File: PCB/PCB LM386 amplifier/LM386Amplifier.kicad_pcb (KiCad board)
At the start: 2 copper layers, 37.5 x 25.4 mm, 21 parts, among them J1 JACK_2P, P1 CONN_01X02, P2 CONN_01X02, U1 LM386

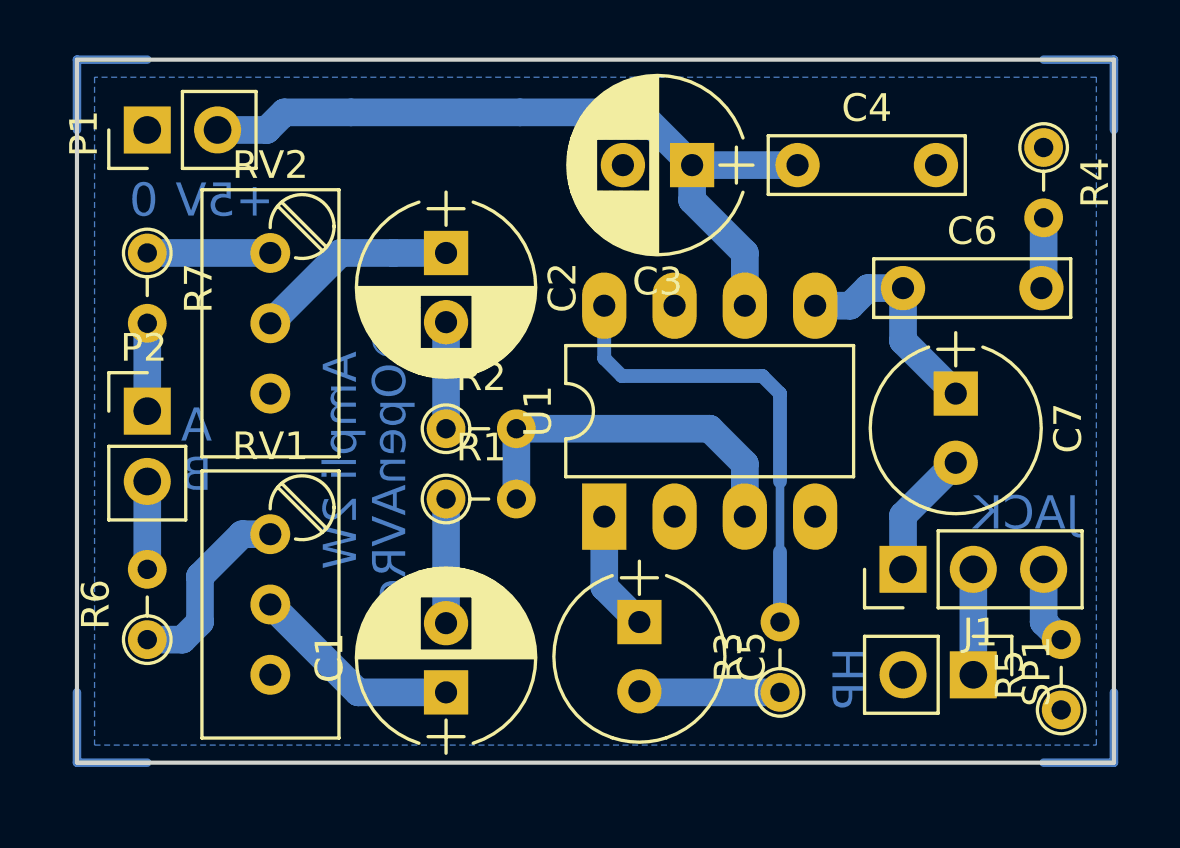
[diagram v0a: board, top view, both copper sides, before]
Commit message: Update pcb board
Add capacitor on pin 7.
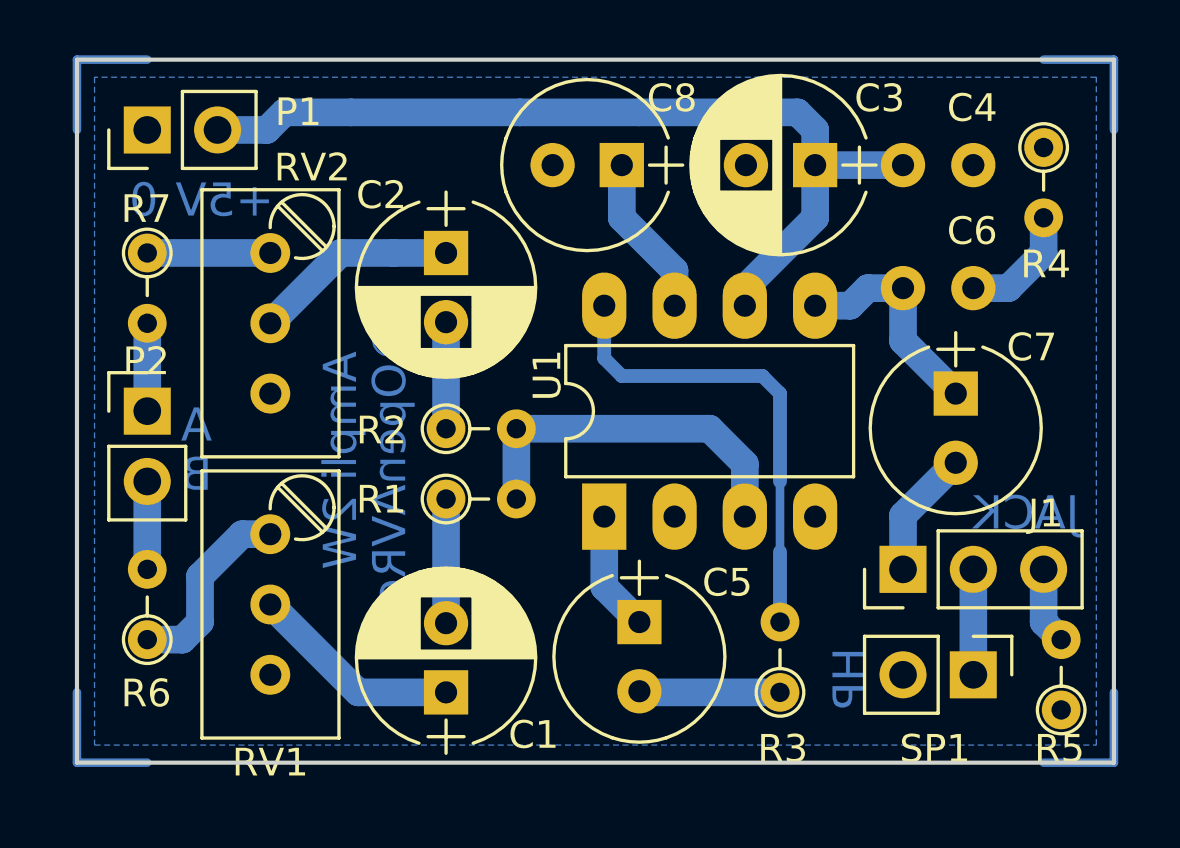
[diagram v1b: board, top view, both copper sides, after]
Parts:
- added C8: 10µF, Capacitors_THT:CP_Radial_Tantal_D6.0mm_P2.50mm, F.Cu at (150.5, 81.3)
- moved C3 4.44 mm to (157.5, 81.3)
- moved C4 3.81 mm to (160.7, 81.3)
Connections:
- U1 pad 7: (no net) -> Net-(C8-Pad1)
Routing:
- net Net-(C8-Pad1): track 0.00 -> 5.87 mm
- net +5V: track 27.9 -> 32.7 mm
- net Net-(C6-Pad2): track 2.57 -> 4.45 mm
